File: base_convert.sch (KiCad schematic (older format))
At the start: 14 parts, among them J1 ISP, J2 Extra, Q1 Q_PMOS_GSD, SW2 SELECT

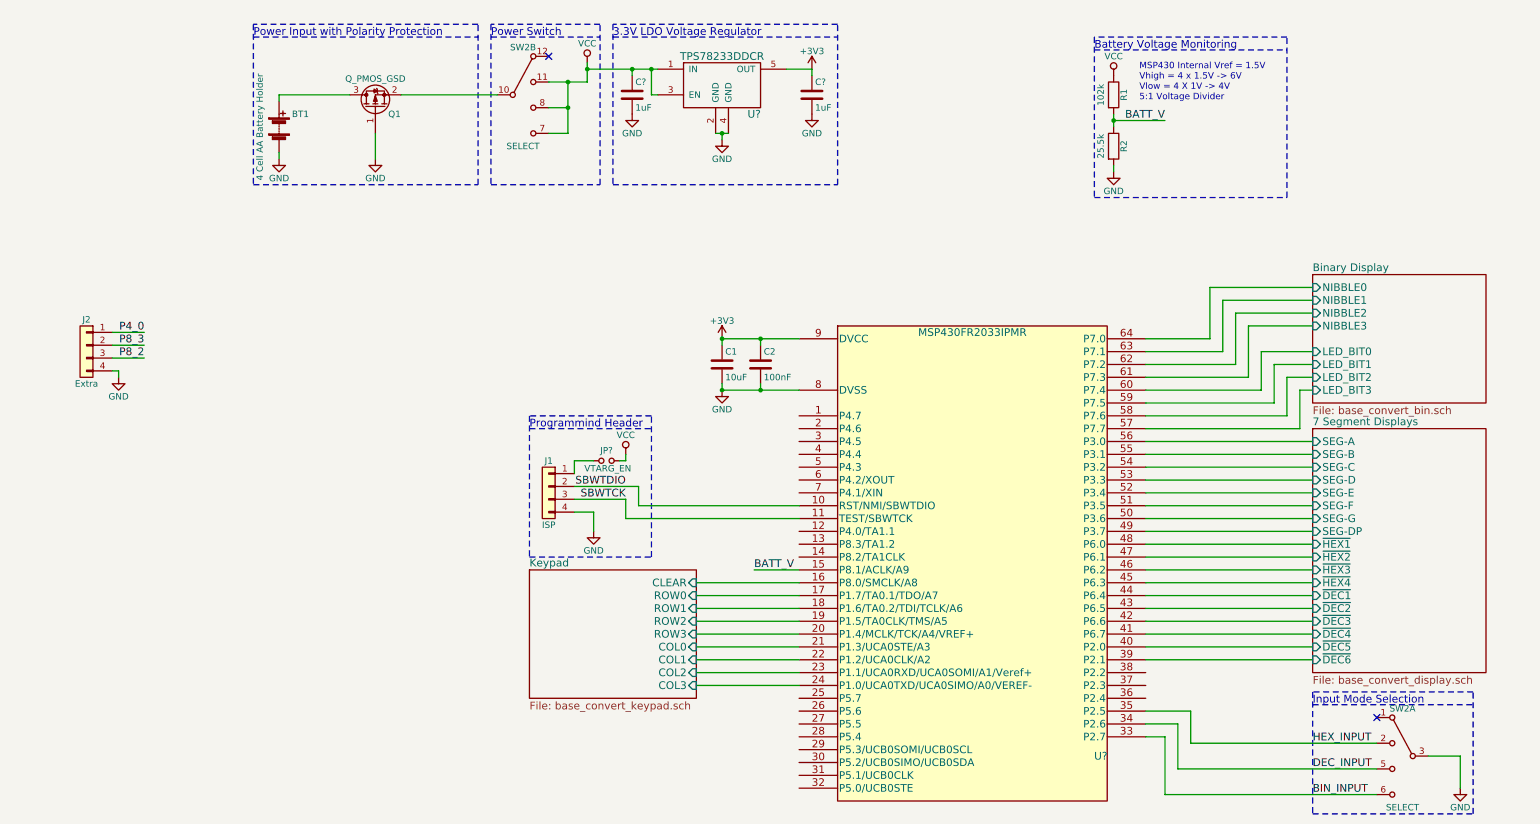
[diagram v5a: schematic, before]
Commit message: renamed digit control lines
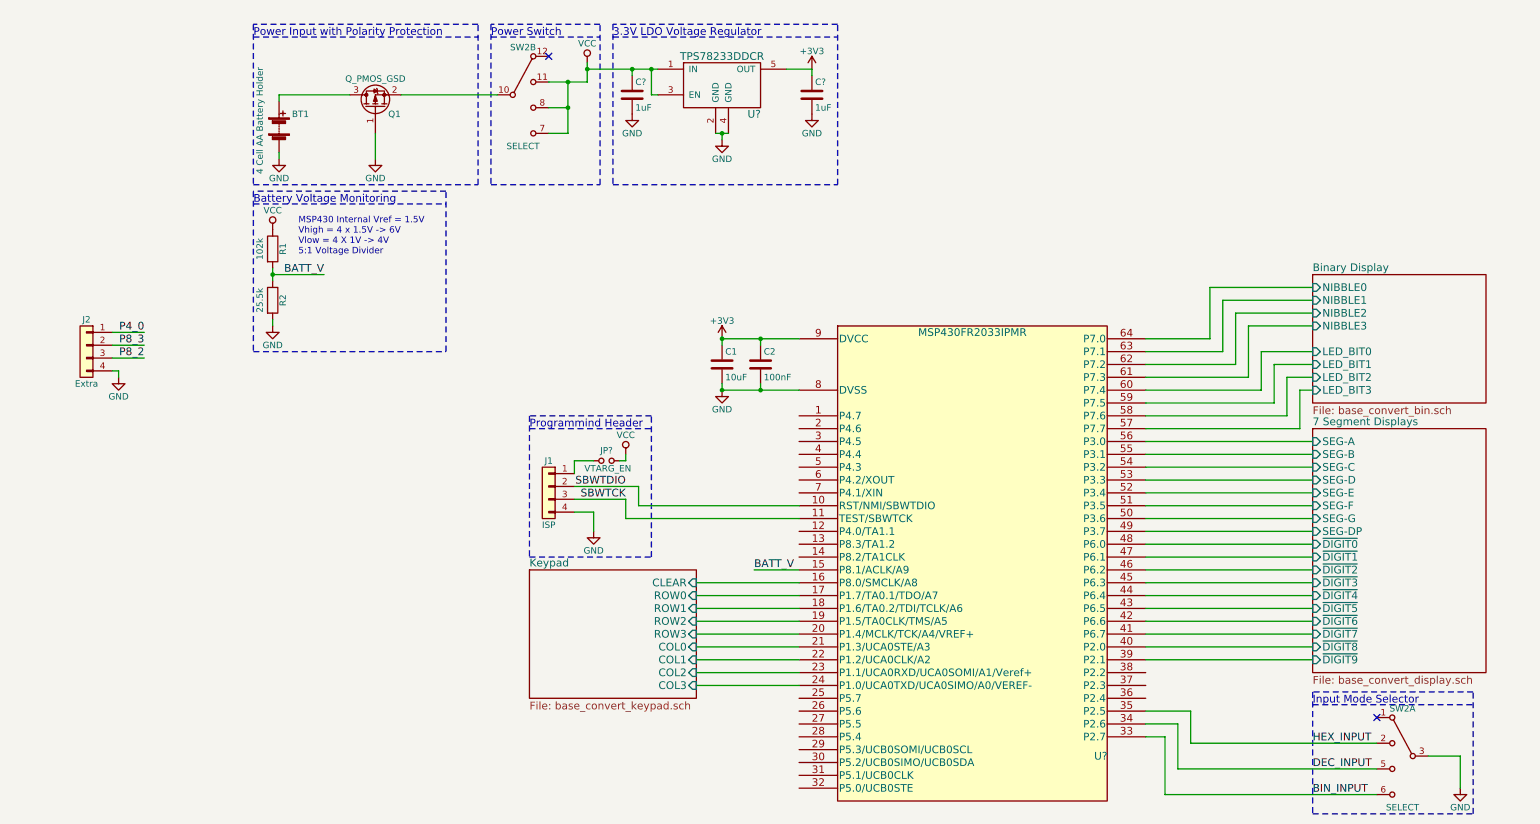
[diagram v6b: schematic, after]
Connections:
- net 7 Segment Displays/~DEC1 renamed 7 Segment Displays/~DIGIT4
- net 7 Segment Displays/~DEC2 renamed 7 Segment Displays/~DIGIT5
- net 7 Segment Displays/~DEC3 renamed 7 Segment Displays/~DIGIT6
- net 7 Segment Displays/~DEC4 renamed 7 Segment Displays/~DIGIT7
- net 7 Segment Displays/~DEC5 renamed 7 Segment Displays/~DIGIT8
- net 7 Segment Displays/~DEC6 renamed 7 Segment Displays/~DIGIT9
- net 7 Segment Displays/~HEX1 renamed 7 Segment Displays/~DIGIT0
- net 7 Segment Displays/~HEX2 renamed 7 Segment Displays/~DIGIT1
- net 7 Segment Displays/~HEX3 renamed 7 Segment Displays/~DIGIT2
- net 7 Segment Displays/~HEX4 renamed 7 Segment Displays/~DIGIT3
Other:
- note added: "Input Mode Selector"
- note removed: "Input Mode Selection"
- moved on the sheet: R1, R2
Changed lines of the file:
@@
 $EndDescr
-$Sheet
-S 9050 3700 1350 1900
-U 5AEA74C1
-F0 "7 Segment Displays" 60
-F1 "base_convert_display.sch" 60
-F2 "SEG-A" I L 9050 3800 60
-F3 "SEG-B" I L 9050 3900 60
-F4 "SEG-C" I L 9050 4000 60
-F5 "SEG-D" I L 9050 4100 60
-F6 "SEG-E" I L 9050 4200 60
-F7 "SEG-F" I L 9050 4300 60
-F8 "SEG-G" I L 9050 4400 60
-F9 "SEG-DP" I L 9050 4500 60
-F10 "~HEX1" I L 9050 4600 60
-F11 "~HEX2" I L 9050 4700 60
-F12 "~HEX3" I L 9050 4800 60
-F13 "~HEX4" I L 9050 4900 60
-F14 "~DEC1" I L 9050 5000 60
-F15 "~DEC2" I L 9050 5100 60
-F16 "~DEC3" I L 9050 5200 60
-F17 "~DEC4" I L 9050 5300 60
-F18 "~DEC5" I L 9050 5400 60
-F19 "~DEC6" I L 9050 5500 60
-$EndSheet
 $Sheet
 S 9050 2500 1350 1000
@@
 P 1000 1350
 F 0 "BT1" H 1100 1450 50  0000 L CNN
-F 1 "4 Cell AA Battery Holder" V 850 1350 50  0000 C CNN
+F 1 "4 Cell AA Battery Holder" V 850 1400 50  0000 C CNN
 F 2 "MPD:BC4AAPC" V 1000 1410 50  0001 C CNN
 F 3 "http://www.memoryprotectiondevices.com/datasheets/BC4AAPC-datasheet.pdf" V 1000 1410 50  0001 C CNN
@@
 L R R1
 U 1 1 5AF2F1FC
-P 7500 1100
-F 0 "R1" V 7580 1100 50  0000 C CNN
-F 1 "102k" V 7400 1100 50  0000 C CNN
-F 2 "Resistors_SMD:R_0805" V 7430 1100 50  0001 C CNN
-F 3 "" H 7500 1100 50  0001 C CNN
-F 4 "NONE" H 7500 1100 60  0001 C CNN "Manufacture"
-F 5 "NONE" H 7500 1100 60  0001 C CNN "Mfg Part Number"
-F 6 "NONE" H 7500 1100 60  0001 C CNN "Package"
-F 7 "NONE" H 7500 1100 60  0001 C CNN "Description"
-	1    7500 1100
+P 950 2300
+F 0 "R1" V 1030 2300 50  0000 C CNN
+F 1 "102k" V 850 2300 50  0000 C CNN
+F 2 "Resistors_SMD:R_0805" V 880 2300 50  0001 C CNN
+F 3 "" H 950 2300 50  0001 C CNN
+F 4 "NONE" H 950 2300 60  0001 C CNN "Manufacture"
+F 5 "NONE" H 950 2300 60  0001 C CNN "Mfg Part Number"
+F 6 "NONE" H 950 2300 60  0001 C CNN "Package"
+F 7 "NONE" H 950 2300 60  0001 C CNN "Description"
+	1    950  2300
 	1    0    0    -1
 $EndComp
@@
 L R R2
 U 1 1 5AF2FAFB
-P 7500 1500
-F 0 "R2" V 7580 1500 50  0000 C CNN
-F 1 "25.5k" V 7400 1500 50  0000 C CNN
-F 2 "Resistors_SMD:R_0805" V 7430 1500 50  0001 C CNN
-F 3 "" H 7500 1500 50  0001 C CNN
-F 4 "NONE" H 7500 1500 60  0001 C CNN "Manufacture"
-F 5 "NONE" H 7500 1500 60  0001 C CNN "Mfg Part Number"
-F 6 "NONE" H 7500 1500 60  0001 C CNN "Package"
-F 7 "NONE" H 7500 1500 60  0001 C CNN "Description"
-	1    7500 1500
+P 950 2700
+F 0 "R2" V 1030 2700 50  0000 C CNN
+F 1 "25.5k" V 850 2700 50  0000 C CNN
+F 2 "Resistors_SMD:R_0805" V 880 2700 50  0001 C CNN
+F 3 "" H 950 2700 50  0001 C CNN
+F 4 "NONE" H 950 2700 60  0001 C CNN "Manufacture"
+F 5 "NONE" H 950 2700 60  0001 C CNN "Mfg Part Number"
+F 6 "NONE" H 950 2700 60  0001 C CNN "Package"
+F 7 "NONE" H 950 2700 60  0001 C CNN "Description"
+	1    950  2700
 	1    0    0    -1
 $EndComp
@@
 L GND #PWR7
 U 1 1 5AF3048A
-P 7500 1700
-F 0 "#PWR7" H 7500 1450 50  0001 C CNN
-F 1 "GND" H 7500 1550 50  0000 C CNN
-F 2 "" H 7500 1700 50  0001 C CNN
-F 3 "" H 7500 1700 50  0001 C CNN
-	1    7500 1700
+P 950 2900
+F 0 "#PWR7" H 950 2650 50  0001 C CNN
+F 1 "GND" H 950 2750 50  0000 C CNN
+F 2 "" H 950 2900 50  0001 C CNN
+F 3 "" H 950 2900 50  0001 C CNN
+	1    950  2900
 	1    0    0    -1
 $EndComp
@@
 Text Label 9050 6550 0    60   ~ 0
 BIN_INPUT
-Text Label 7900 1300 2    60   ~ 0
+Text Label 1350 2500 2    60   ~ 0
 BATT_V
 Text Label 3700 4150 2    60   ~ 0
@@
 L VCC #PWR?
 U 1 1 5B28B1DA
-P 7500 950
-F 0 "#PWR?" H 7500 800 50  0001 C CNN
-F 1 "VCC" H 7500 1100 50  0000 C CNN
-F 2 "" H 7500 950 50  0001 C CNN
-F 3 "" H 7500 950 50  0001 C CNN
-	1    7500 950
+P 950 2150
+F 0 "#PWR?" H 950 2000 50  0001 C CNN
+F 1 "VCC" H 950 2300 50  0000 C CNN
+F 2 "" H 950 2150 50  0001 C CNN
+F 3 "" H 950 2150 50  0001 C CNN
+	1    950  2150
 	1    0    0    -1
 $EndComp
@@
 	10200 6250 9950 6250
 Wire Wire Line
-	7500 1700 7500 1650
-Wire Wire Line
-	7500 1250 7500 1350
-Wire Wire Line
-	7500 1300 7900 1300
+	950  2900 950  2850
+Wire Wire Line
+	950  2450 950  2550
+Wire Wire Line
+	950  2500 1350 2500
 Wire Wire Line
 	3300 4350 3450 4350
@@
 Connection ~ 4750 3400
 Connection ~ 4450 3000
-Connection ~ 7500 1300
+Connection ~ 950  2500
 Connection ~ 3250 1000
 Connection ~ 3250 1200
@@
 	8100 6150 8100 5900
 Text Notes 9050 5850 0    60   ~ 0
-Input Mode Selection
+Input Mode Selector
 Wire Notes Line
 	9050 5750 9050 6700
@@
 Wire Wire Line
 	3800 4300 5050 4300
-Text Notes 7700 1150 0    50   ~ 0
+Text Notes 1150 2350 0    50   ~ 0
 MSP430 Internal Vref = 1.5V\nVhigh = 4 x 1.5V -> 6V\nVlow = 4 X 1V -> 4V\n5:1 Voltage Divider
-Text Notes 7350 750  0    60   ~ 0
+Text Notes 800  1950 0    60   ~ 0
 Battery Voltage Monitoring
 Wire Notes Line
-	7350 650  7350 1900
-Wire Notes Line
-	7350 1900 8850 1900
-Wire Notes Line
-	8850 1900 8850 650
-Wire Notes Line
-	8850 650  7350 650
-Wire Notes Line
-	7350 750  8850 750
+	800  1850 800  3100
+Wire Notes Line
+	800  3100 2300 3100
+Wire Notes Line
+	2300 3100 2300 1850
+Wire Notes Line
+	2300 1850 800  1850
+Wire Notes Line
+	800  1950 2300 1950
 Text Label 4700 4800 0    60   ~ 0
 BATT_V
 Wire Wire Line
 	4700 4800 5050 4800
+$Sheet
+S 9050 3700 1350 1900
+U 5AEA74C1
+F0 "7 Segment Displays" 60
+F1 "base_convert_display.sch" 60
+F2 "SEG-A" I L 9050 3800 60
+F3 "SEG-B" I L 9050 3900 60
+F4 "SEG-C" I L 9050 4000 60
+F5 "SEG-D" I L 9050 4100 60
+F6 "SEG-E" I L 9050 4200 60
+F7 "SEG-F" I L 9050 4300 60
+F8 "SEG-G" I L 9050 4400 60
+F9 "SEG-DP" I L 9050 4500 60
+F10 "~DIGIT0" I L 9050 4600 60
+F11 "~DIGIT1" I L 9050 4700 60
+F12 "~DIGIT2" I L 9050 4800 60
+F13 "~DIGIT3" I L 9050 4900 60
+F14 "~DIGIT4" I L 9050 5000 60
+F15 "~DIGIT5" I L 9050 5100 60
+F16 "~DIGIT6" I L 9050 5200 60
+F17 "~DIGIT7" I L 9050 5300 60
+F18 "~DIGIT8" I L 9050 5400 60
+F19 "~DIGIT9" I L 9050 5500 60
+$EndSheet
 $EndSCHEMATC

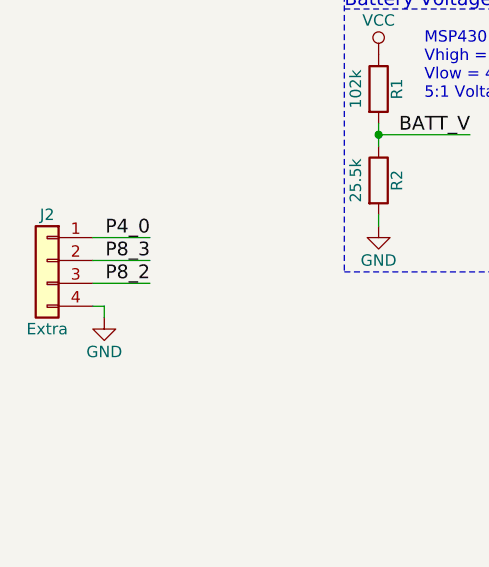
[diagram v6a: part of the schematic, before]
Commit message: removed extra pin header
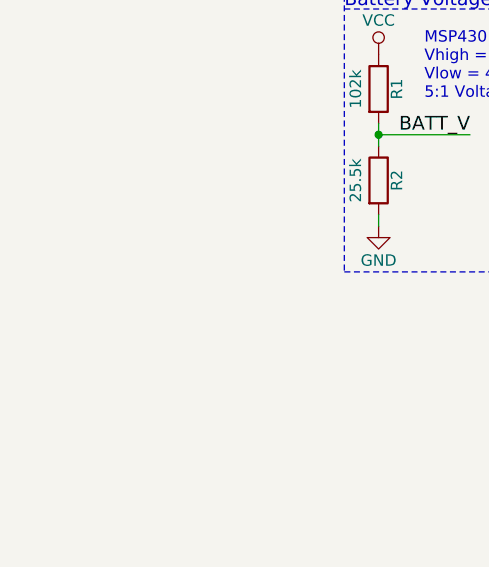
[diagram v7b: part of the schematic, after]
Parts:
- removed J2: Extra, Pin_Headers:Pin_Header_Straight_1x04_Pitch2.54mm, symbol Conn_01x04
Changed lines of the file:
@@
-	1    0    0    -1
-$EndComp
-$Comp
-L GND #PWR4
-U 1 1 5AFB7D7E
-P -250 3300
-F 0 "#PWR4" H -250 3050 50  0001 C CNN
-F 1 "GND" H -250 3150 50  0000 C CNN
-F 2 "" H -250 3300 50  0001 C CNN
-F 3 "" H -250 3300 50  0001 C CNN
-	1    -250 3300
 	1    0    0    -1
 $EndComp
@@
 Text Label 3700 4250 2    60   ~ 0
 SBWTCK
-Text Label -50  2950 2    60   ~ 0
-P4_0
-Text Label -50  3050 2    60   ~ 0
-P8_3
-Text Label -50  3150 2    60   ~ 0
-P8_2
 NoConn ~ 3100 800
 NoConn ~ 9550 5950
@@
 $EndComp
 $Comp
-L Conn_01x04 J2
-U 1 1 5AFB5A51
-P -500 3050
-F 0 "J2" H -500 3250 50  0000 C CNN
-F 1 "Extra" H -500 2750 50  0000 C CNN
-F 2 "Pin_Headers:Pin_Header_Straight_1x04_Pitch2.54mm" H -500 3050 50  0001 C CNN
-F 3 "" H -500 3050 50  0001 C CNN
-	1    -500 3050
-	-1   0    0    -1
-$EndComp
-$Comp
 L MSP430FR2033IPMR U?
 U 1 1 5B2ADB04
@@
 	8100 5900 7750 5900
 Wire Wire Line
-	-50  2950 -300 2950
-Wire Wire Line
-	-50  3050 -300 3050
-Wire Wire Line
-	-50  3150 -300 3150
-Wire Wire Line
-	-300 3250 -250 3250
-Wire Wire Line
-	-250 3250 -250 3300
-Wire Wire Line
 	4250 4900 5050 4900
